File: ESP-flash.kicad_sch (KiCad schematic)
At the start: 23 parts, among them J101 USB_B_Micro, J102 USB_C_Receptacle_USB2.0, J103 Conn_01x06, Q101 MMDT3904, SW101 SW_SPDT, U101 SESRV05-4, U102 TLV75533PDBV, U103 CH340C

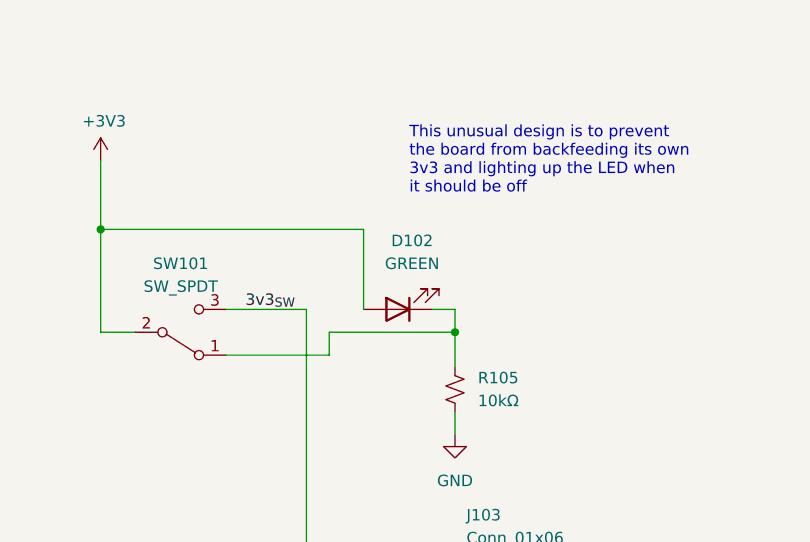
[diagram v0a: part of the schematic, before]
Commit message: Substitute out-of-stock components
Unsurprising considering how long ago this was last ordered, some of the
components were no longer stocked.
- Green LED (already had a replacement, in other PCB designs)
- Polyfuse (easily found another one on JLCPCB)
- The SPDT switch (couldn't find an exact replacement, and ended up
  using another type with a already-available footprint).
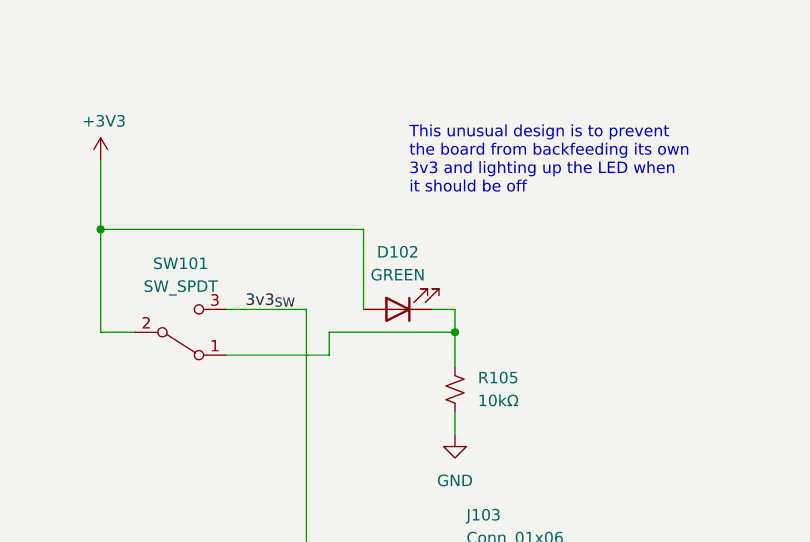
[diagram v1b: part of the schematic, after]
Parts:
- D102, D103: LCSC C72043 -> C779453
- F101: LCSC C261942 -> C516070
- SW101: footprint Button_Switch_SMD:SW_SPDT_CK-JS102011SAQN -> Button_Switch_SMD:SW_SPDT_PCM12; JLCPCB_CORRECTION 0;-2.75;180 -> (none); LCSC C125040 -> C221841

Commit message: Move USB section into subsheet
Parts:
- removed F101: 0ZCK0050FF2E (TLC-PSMD050), Fuse:Fuse_0805_2012Metric_Pad1.15x1.40mm_HandSolder, symbol Device:Polyfuse
- removed J101: USB_B_Micro, Connector_USB_custom:USB_Micro-B_Amphenol_10118194_Horizontal, symbol Connector:USB_B_Micro
- removed J102: USB_C_Receptacle_USB2.0, Connector_USB:USB_C_Receptacle_HRO_TYPE-C-31-M-12, symbol Connector:USB_C_Receptacle_USB2.0
- removed R101, R102: 5.1k, Resistor_SMD:R_0603_1608Metric, symbol Device:R_US
- removed U101: SESRV05-4, Package_TO_SOT_SMD:SOT-23-6, symbol Power_Protection_custom:SESRV05-4
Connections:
- net USB_D+ renamed USB/USB_D+
- net USB_D- renamed USB/USB_D-
- no-connect marks 10 -> 5
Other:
- added sheet USB (subsheet/usb.kicad_sch)
